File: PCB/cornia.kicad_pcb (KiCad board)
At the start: 2 copper layers, 159.3 x 108.3 mm, 67 parts, among them SW1 SW_Push, SW10 SW_Push, SW11 SW_Push, SW12 SW_Push, SW13 SW_Push, SW14 SW_Push, SW15 SW_Push, SW16 SW_Push, SW17 SW_Push, SW18 SW_Push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

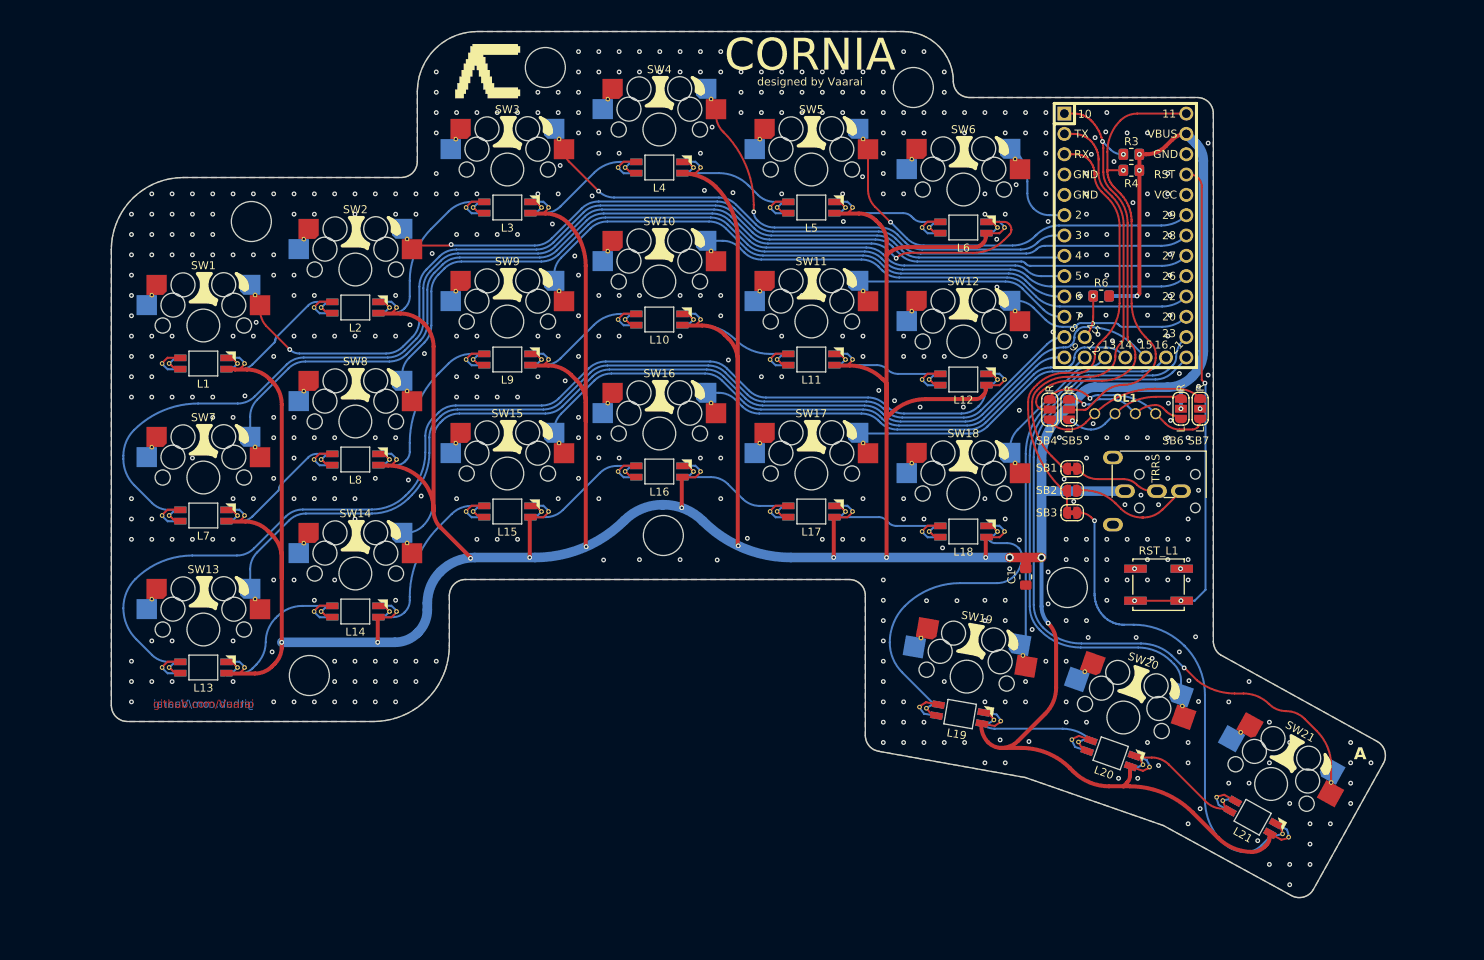
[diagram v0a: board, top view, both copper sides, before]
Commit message: [PCB] Rework OLED SBx & Add last led DOUT TP
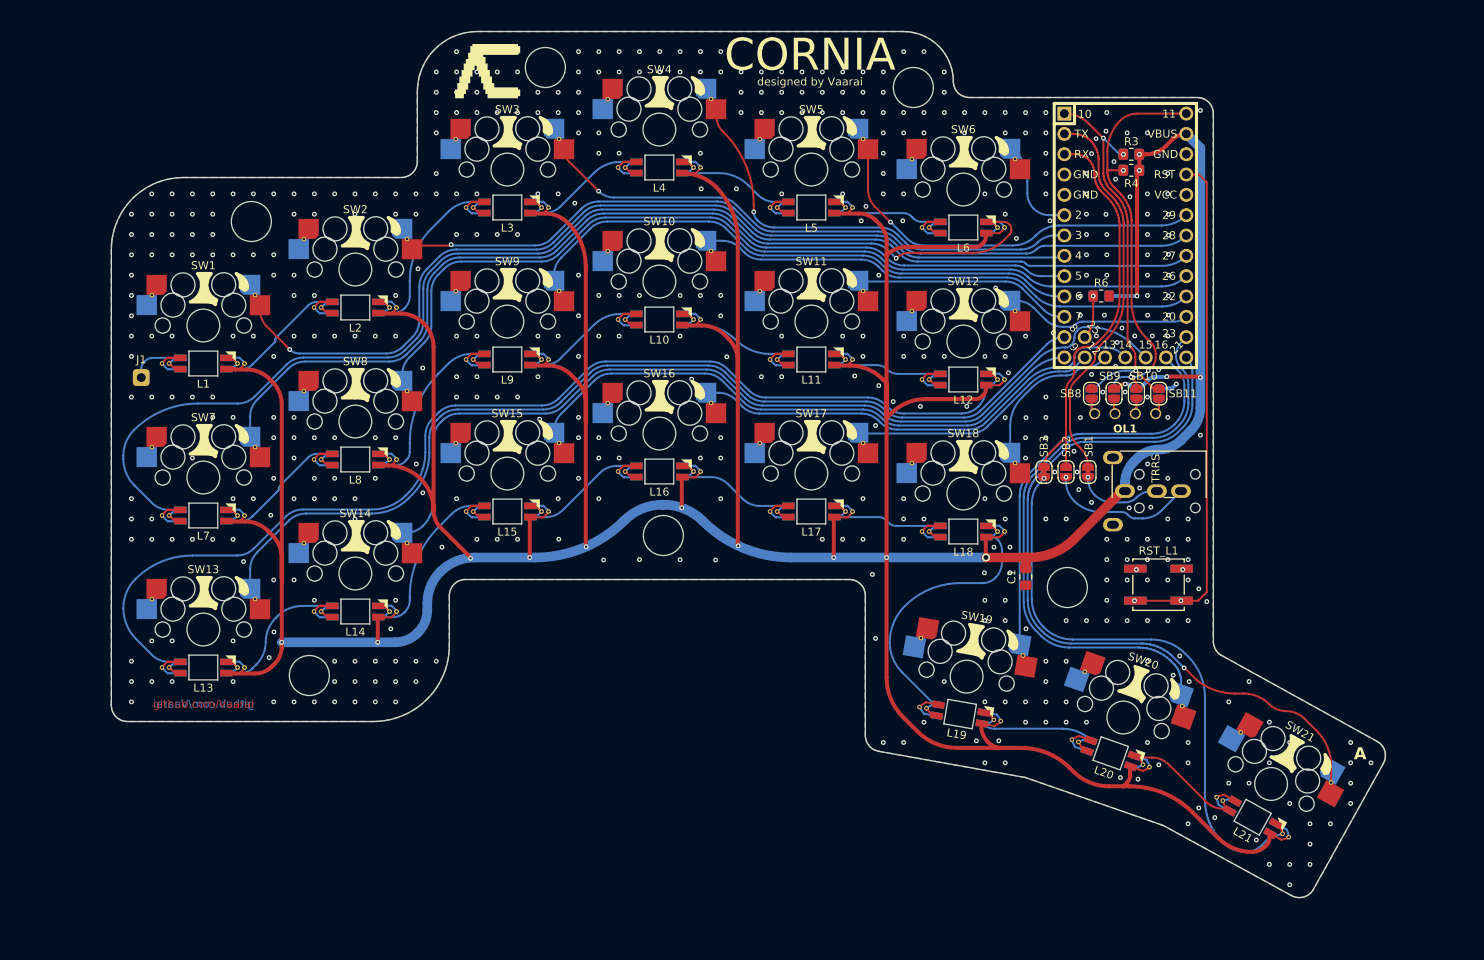
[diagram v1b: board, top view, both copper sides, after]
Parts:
- added J1: Conn_01x01_Pin, cornia-footprints:1Pin, F.Cu at (22.4, 61.2)
- added SB10: SB, cornia-footprints:SolderJumper-2_Open, F.Cu at (146.8, 63.2)
- added SB11: SB, cornia-footprints:SolderJumper-2_Open, F.Cu at (149.6, 63.2)
- added SB8: SB, cornia-footprints:SolderJumper-2_Open, F.Cu at (141.2, 63.2)
- added SB9: SB, cornia-footprints:SolderJumper-2_Open, F.Cu at (144.0, 63.2)
- SB4, SB5, SB6, SB7: footprint cornia-footprints:SolderJumper-3 -> cornia-footprints:SolderJumper-2_Open; moved to B.Cu
- moved SB3 6.19 mm to (135.2, 73.0), turned to -90 degrees
- moved SB5 5.97 mm to (144.0, 63.2), turned to -90 degrees
- moved SB6 5.88 mm to (146.8, 63.2), turned to -90 degrees
- moved SB4 5.60 mm to (141.2, 63.2), turned to -90 degrees
- moved SB7 5.50 mm to (149.6, 63.2), turned to -90 degrees
- moved SB2 2.46 mm to (138.0, 73.0), turned to -90 degrees
- moved SB1 2.02 mm to (140.8, 73.0), turned to -90 degrees
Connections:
- net Net-(U1-25) renamed /Handedness
- L1 pad 1: unconnected-(L1-DOUT-Pad1)_2 -> Net-(J1-Pin_1)
- SB4 pad 1: Net-(OL1-SDA) -> /SDA
- SB4 pad 2: /SDA -> Net-(OL1-SDA)
- SB5 pad 1: Net-(OL1-SCL) -> /SCL
- SB5 pad 2: /SCL -> Net-(OL1-SCL)
- SB6 pad 1: Net-(OL1-VCC) -> VBUS
- SB6 pad 2: VBUS -> Net-(OL1-VCC)
- SB7 pad 1: Net-(OL1-GND) -> GND
- SB7 pad 2: GND -> Net-(OL1-GND)
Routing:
- net Net-(OL1-GND): track 21.9 -> 4.04 mm, vias 1 -> 0
- net Net-(OL1-SDA): track 21.3 -> 4.08 mm
- net Net-(OL1-VCC): track 15.9 -> 3.83 mm, vias 1 -> 0
- net Net-(OL1-SCL): track 15.7 -> 3.82 mm, vias 1 -> 0
- net /LED: track 59.1 -> 70.5 mm
- net Net-(J1-Pin_1): track 0.00 -> 6.71 mm
- net /TX: track 55.0 -> 48.3 mm
- net /RX_LED: track 56.5 -> 50.5 mm
- net /SDA: track 55.1 -> 49.6 mm, vias 2 -> 3
- net /SCL: track 55.9 -> 51.3 mm, vias 1 -> 3
- net Net-(L18-DIN): track 38.3 -> 34.2 mm
- net /In_SW19: track 48.0 -> 51.6 mm
- net /In_SW20: track 72.0 -> 75.3 mm
- net Net-(SB2-B): track 15.1 -> 18.4 mm, vias 0 -> 1
- net /In_SW21: track 92.3 -> 94.8 mm
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
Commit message: [PCB] Move 2mm left MCU/TRRS/RST
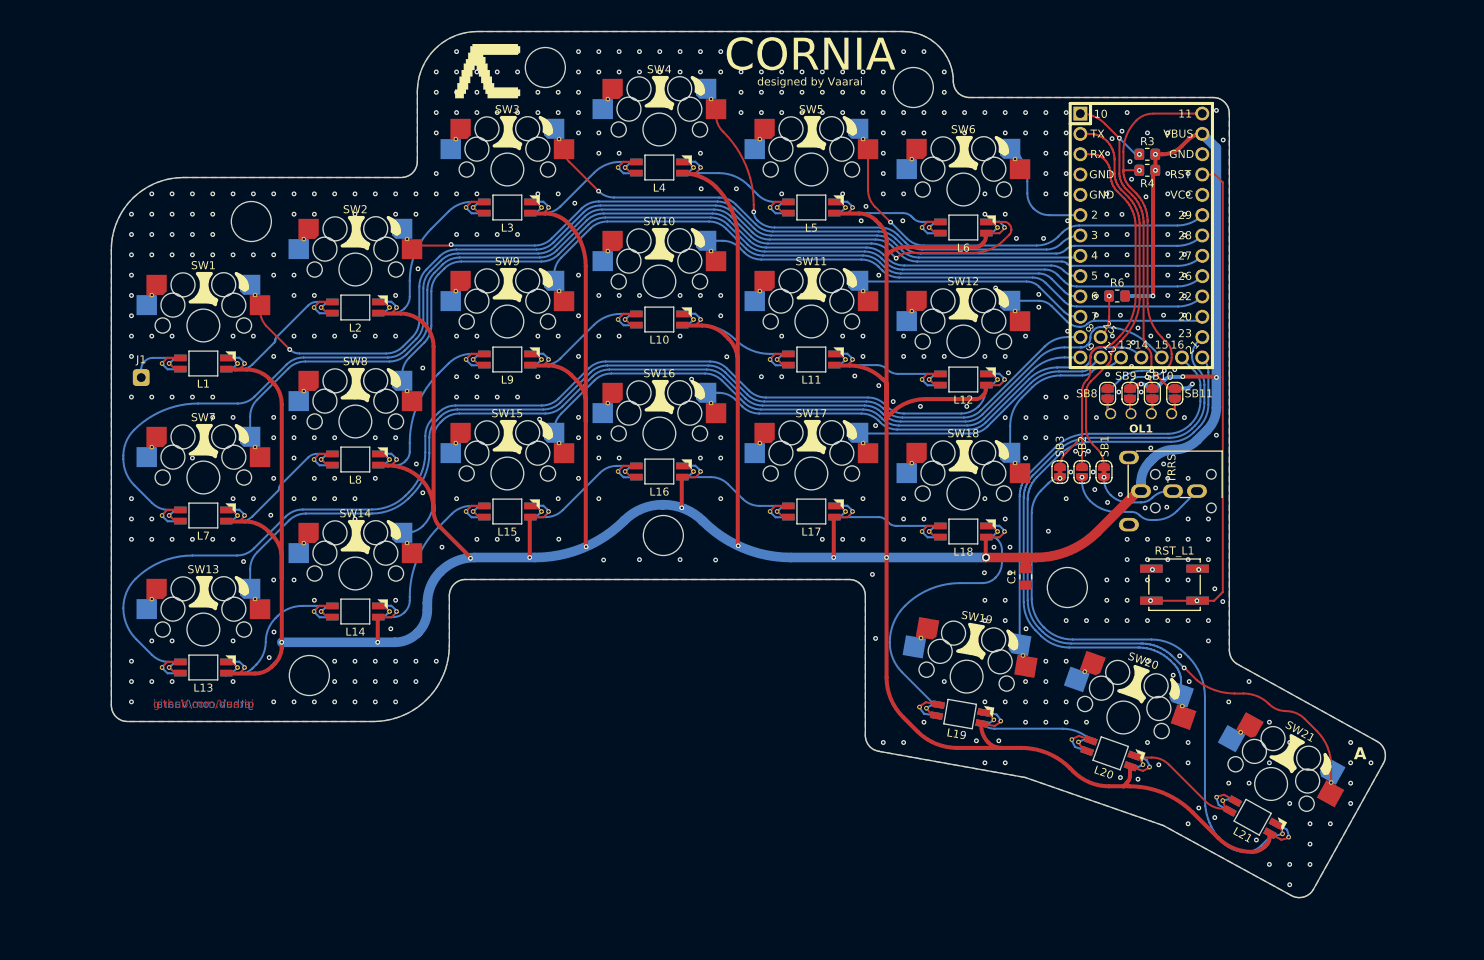
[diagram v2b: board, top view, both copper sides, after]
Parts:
- moved OL1 2.00 mm to (147.4, 65.7)
- moved R1 2.00 mm to (148.2, 33.3)
- moved R2 2.00 mm to (148.2, 35.3)
- moved R3 2.00 mm to (148.2, 33.3)
- moved R4 2.00 mm to (148.2, 35.3)
- moved R5 2.00 mm to (144.4, 51.0)
- moved R6 2.00 mm to (144.4, 51.0)
- moved RST_L1 2.00 mm to (151.6, 87.1)
- moved RST_R1 2.00 mm to (151.6, 87.1)
- moved SB1 2.00 mm to (142.8, 73.0)
- moved SB10 2.00 mm to (148.8, 63.2)
- moved SB11 2.00 mm to (151.6, 63.2)
- moved SB2 2.00 mm to (140.0, 73.0)
- moved SB3 2.00 mm to (137.2, 73.0)
- moved SB4 2.00 mm to (143.2, 63.2)
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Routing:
- net /In_SW9: track 70.7 -> 72.8 mm
- net /In_SW12: track 23.4 -> 25.6 mm
- net /In_SW8: track 113.7 -> 115.8 mm
- net /In_SW10: track 62.8 -> 64.9 mm
- net /In_SW11: track 27.4 -> 29.4 mm
- net /In_SW5: track 49.2 -> 51.2 mm
- net /In_SW16: track 58.3 -> 60.3 mm
- net /In_SW7: track 120.8 -> 122.8 mm
- net /In_SW2: track 86.2 -> 88.2 mm
- net /In_SW18: track 19.2 -> 21.2 mm
- net /In_SW17: track 31.8 -> 33.8 mm
- net /In_SW6: track 12.6 -> 14.6 mm
- net /In_SW14: track 115.0 -> 117.0 mm
- net /In_SW15: track 72.7 -> 74.7 mm
- net /In_SW3: track 83.7 -> 85.7 mm
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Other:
- outline, holes or cut-outs redrawn

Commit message: [PCB/Footprint] Remove 5mm mounting hole + update RP2040 & RST 3D
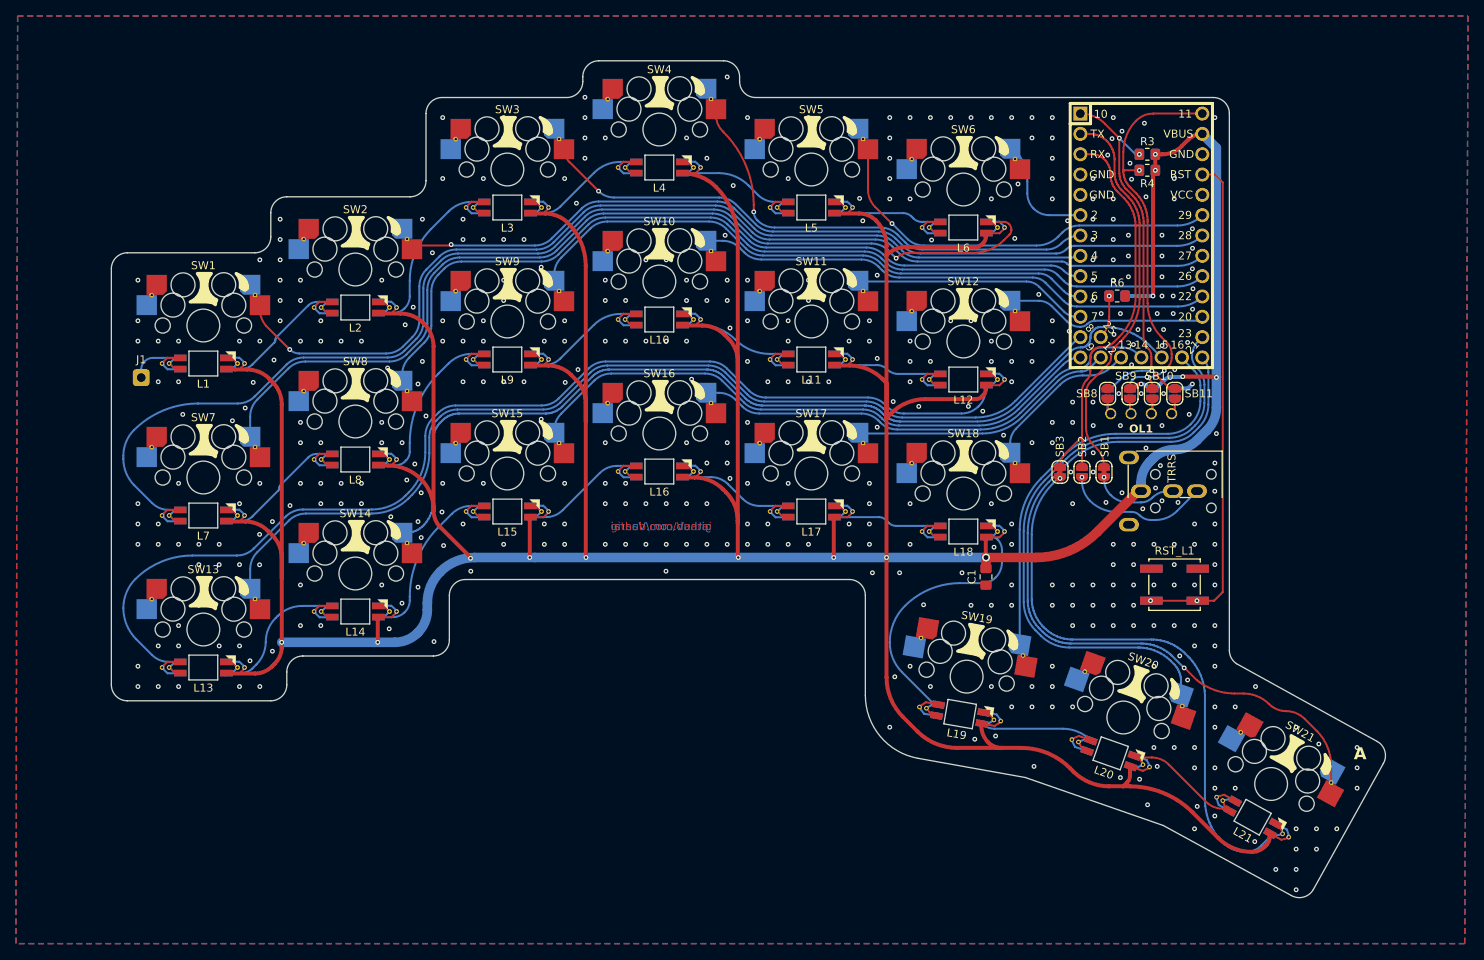
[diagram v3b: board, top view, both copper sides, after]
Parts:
- removed H1, H2, H3, H4, H5, H6: MountingHole, cornia-footprints:MountingHole_5mm
- moved C1 4.97 mm to (128.0, 86.1)
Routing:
- net VBUS: track 627.1 -> 632.9 mm, vias 16 -> 15
- net /In_SW19: track 53.4 -> 51.8 mm
- net /In_SW20: track 77.2 -> 75.6 mm
- net /In_SW21: track 96.7 -> 95.1 mm
- net /In_SW18: track 21.2 -> 19.6 mm
- net GND: vias 535 -> 458
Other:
- board size 159.3 x 108.3 mm -> 159.3 x 104.6 mm
- board text removed: "CORNIA"
- board text removed: "designed by Vaarai"

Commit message: [PCB/Symbol] Add 10x 2.2mm holes + Add new logo
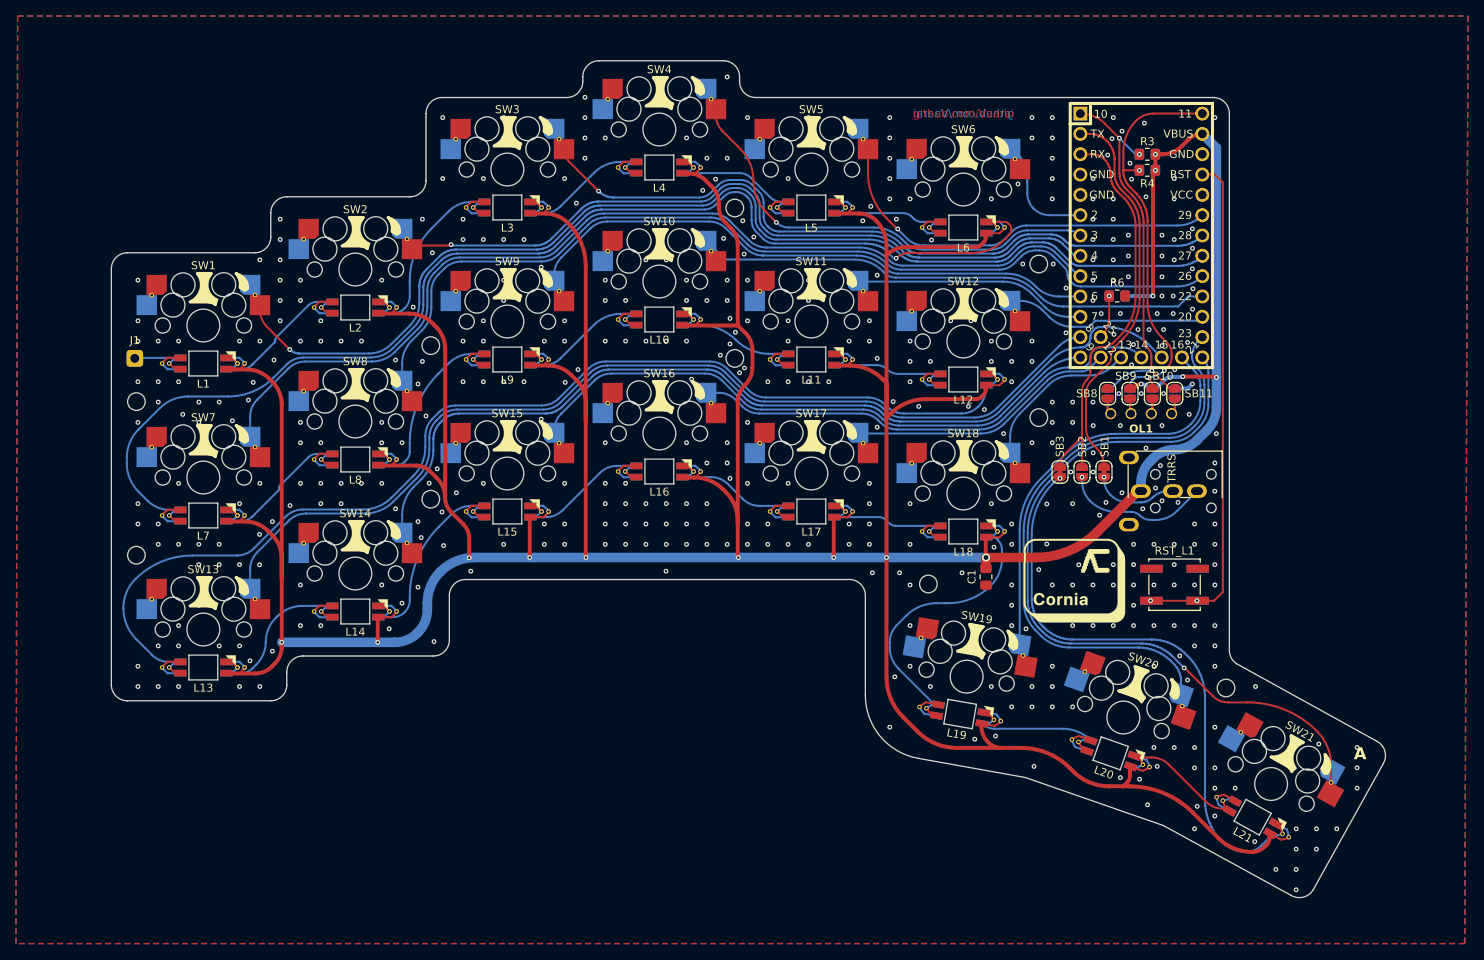
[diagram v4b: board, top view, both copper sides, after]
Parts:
- added H1: Hole, cornia-footprints:MountingHole_2.2mm_M2_no_annular, F.Cu at (21.8, 64.2)
- added H10: Hole, cornia-footprints:MountingHole_2.2mm_M2_no_annular, F.Cu at (158.0, 100.0)
- added H2: Hole, cornia-footprints:MountingHole_2.2mm_M2_no_annular, F.Cu at (21.8, 83.4)
- added H3: Hole, cornia-footprints:MountingHole_2.2mm_M2_no_annular, F.Cu at (58.6, 57.2)
- added H4: Hole, cornia-footprints:MountingHole_2.2mm_M2_no_annular, F.Cu at (58.6, 76.4)
- added H5: Hole, cornia-footprints:MountingHole_2.2mm_M2_no_annular, F.Cu at (96.6, 40.0)
- added H6: Hole, cornia-footprints:MountingHole_2.2mm_M2_no_annular, F.Cu at (96.6, 58.8)
- added H7: Hole, cornia-footprints:MountingHole_2.2mm_M2_no_annular, F.Cu at (134.6, 47.0)
- added H8: Hole, cornia-footprints:MountingHole_2.2mm_M2_no_annular, F.Cu at (134.6, 66.2)
- added H9: Hole, cornia-footprints:MountingHole_2.2mm_M2_no_annular, F.Cu at (120.8, 87.0)
- moved J1 2.53 mm to (21.6, 58.8)
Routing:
- net /In_SW2: track 88.2 -> 93.1 mm
- net /In_SW3: track 85.7 -> 90.0 mm
- net /In_SW1: track 134.6 -> 138.6 mm
- net VBUS: track 632.9 -> 629.6 mm
- net Net-(L6-DIN): track 145.0 -> 147.6 mm
- net /In_SW8: track 115.8 -> 117.9 mm
- net /In_SW14: track 117.2 -> 116.0 mm
- net Net-(J1-Pin_1): track 6.71 -> 5.71 mm
- net /In_SW18: track 19.6 -> 20.4 mm
- net Net-(L12-DIN): track 138.5 -> 137.8 mm
- net /In_SW13: track 125.6 -> 124.8 mm
- net /In_SW4: track 57.1 -> 56.4 mm
- net /In_SW7: track 122.8 -> 123.4 mm
- net GND: vias 458 -> 467

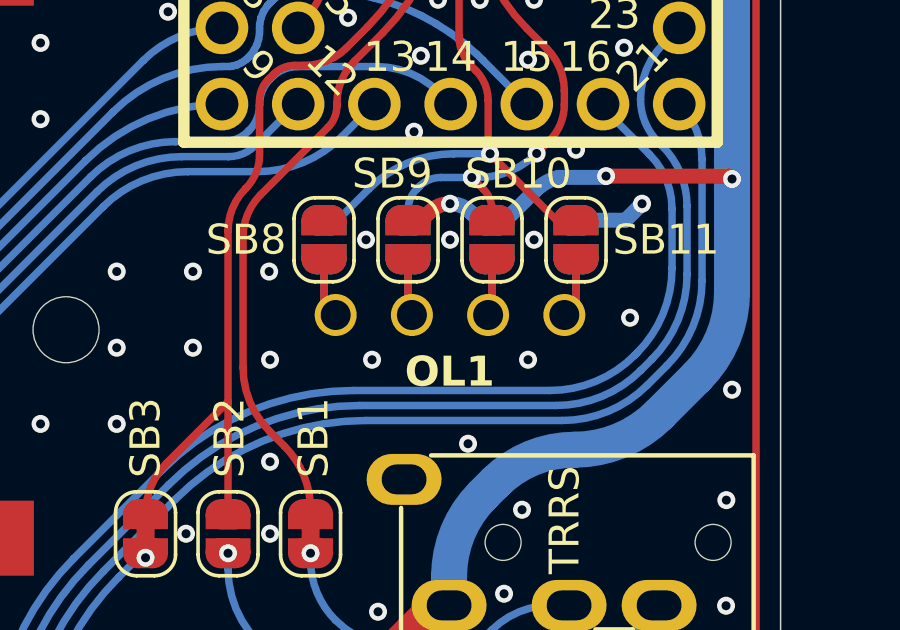
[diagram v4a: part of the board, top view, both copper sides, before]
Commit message: [PCB/Output] Increase Oled pads diameter + update output
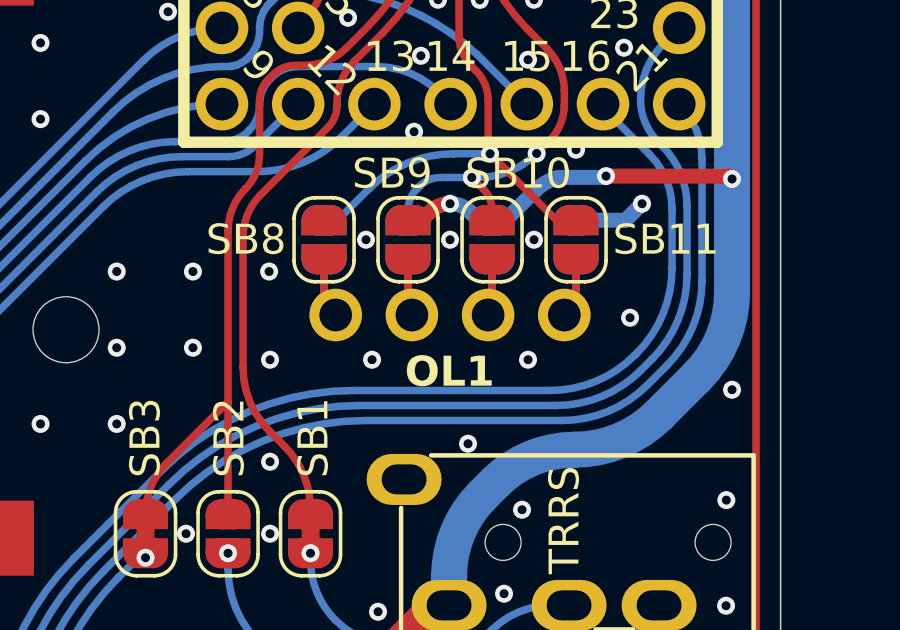
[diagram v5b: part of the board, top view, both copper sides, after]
